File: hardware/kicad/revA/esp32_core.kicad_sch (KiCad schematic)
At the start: 0 parts

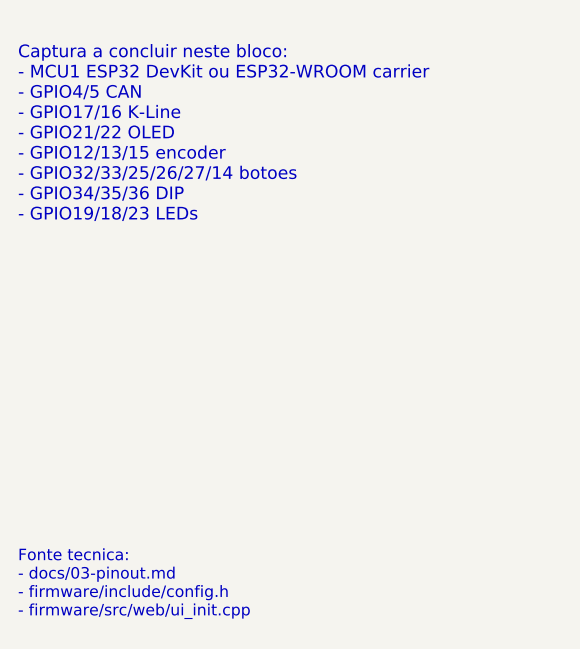
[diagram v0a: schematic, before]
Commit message: feat: persist simulator state and carrier handoff
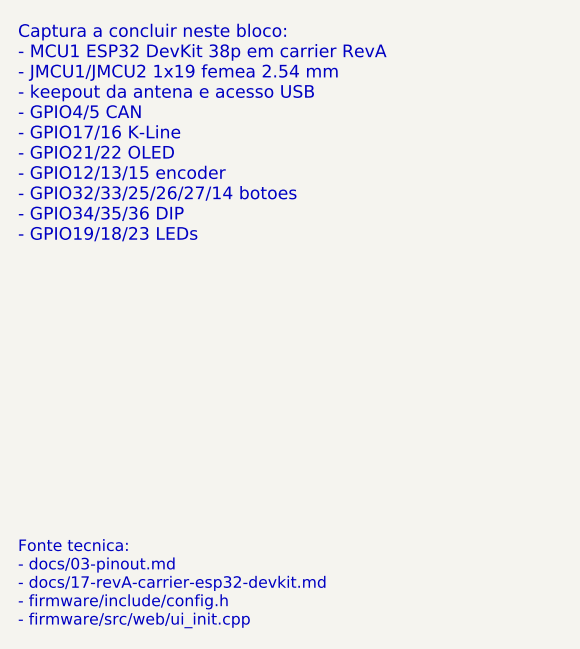
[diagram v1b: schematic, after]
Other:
- note added: "Captura a concluir neste bloco: - MCU1 ESP32 DevKit 38p em carrier RevA - JMCU1/JMCU2 1x19 femea 2.54 mm - keepout da antena e acesso USB - GPIO4/5 CAN - GPIO17/16 K-Line - GPIO21/22 OLED - GPIO12/13/15 encoder - GPIO32/33/25/26/27/14 botoes - GPIO34/35/36 DIP - GPIO19/18/23 LEDs"
- note added: "Fonte tecnica: - docs/03-pinout.md - docs/17-revA-carrier-esp32-devkit.md - firmware/include/config.h - firmware/src/web/ui_init.cpp"
- note removed: "Captura a concluir neste bloco: - MCU1 ESP32 DevKit ou ESP32-WROOM carrier - GPIO4/5 CAN - GPIO17/16 K-Line - GPIO21/22 OLED - GPIO12/13/15 encoder - GPIO32/33/25/26/27/14 botoes - GPIO34/35/36 DIP - GPIO19/18/23 LEDs"
- note removed: "Fonte tecnica: - docs/03-pinout.md - firmware/include/config.h - firmware/src/web/ui_init.cpp"
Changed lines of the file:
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@@
 		(comment 1 "Keep validated GPIO map from firmware/docs")
 	)
-	(text "Captura a concluir neste bloco:\n- MCU1 ESP32 DevKit ou ESP32-WROOM carrier\n- GPIO4/5 CAN\n- GPIO17/16 K-Line\n- GPIO21/22 OLED\n- GPIO12/13/15 encoder\n- GPIO32/33/25/26/27/14 botoes\n- GPIO34/35/36 DIP\n- GPIO19/18/23 LEDs"
+	(text "Captura a concluir neste bloco:\n- MCU1 ESP32 DevKit 38p em carrier RevA\n- JMCU1/JMCU2 1x19 femea 2.54 mm\n- keepout da antena e acesso USB\n- GPIO4/5 CAN\n- GPIO17/16 K-Line\n- GPIO21/22 OLED\n- GPIO12/13/15 encoder\n- GPIO32/33/25/26/27/14 botoes\n- GPIO34/35/36 DIP\n- GPIO19/18/23 LEDs"
 		(exclude_from_sim no)
 		(at 18 20 0)
@@
 		)
 	)
-	(text "Fonte tecnica:\n- docs/03-pinout.md\n- firmware/include/config.h\n- firmware/src/web/ui_init.cpp"
+	(text "Fonte tecnica:\n- docs/03-pinout.md\n- docs/17-revA-carrier-esp32-devkit.md\n- firmware/include/config.h\n- firmware/src/web/ui_init.cpp"
 		(exclude_from_sim no)
 		(at 18 70 0)

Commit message: Align RevA pinout and retire legacy handoff
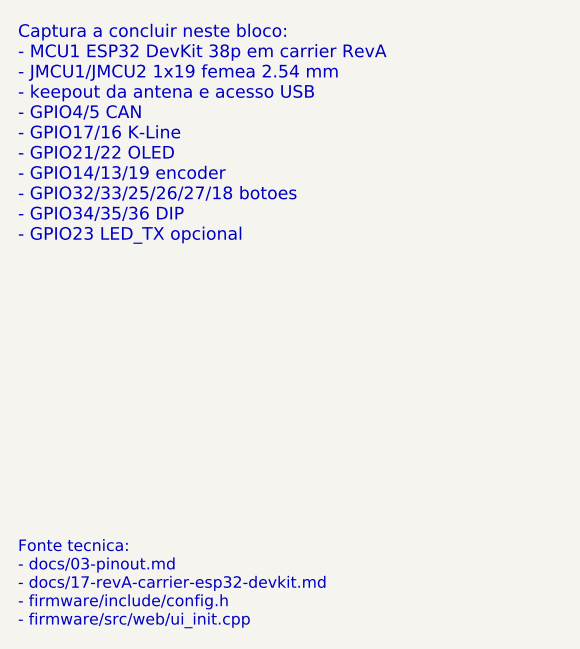
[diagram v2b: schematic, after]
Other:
- note added: "Captura a concluir neste bloco: - MCU1 ESP32 DevKit 38p em carrier RevA - JMCU1/JMCU2 1x19 femea 2.54 mm - keepout da antena e acesso USB - GPIO4/5 CAN - GPIO17/16 K-Line - GPIO21/22 OLED - GPIO14/13/19 encoder - GPIO32/33/25/26/27/18 botoes - GPIO34/35/36 DIP - GPIO23 LED_TX opcional"
- note removed: "Captura a concluir neste bloco: - MCU1 ESP32 DevKit 38p em carrier RevA - JMCU1/JMCU2 1x19 femea 2.54 mm - keepout da antena e acesso USB - GPIO4/5 CAN - GPIO17/16 K-Line - GPIO21/22 OLED - GPIO12/13/15 encoder - GPIO32/33/25/26/27/14 botoes - GPIO34/35/36 DIP - GPIO19/18/23 LEDs"
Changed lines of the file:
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@@
 		(comment 1 "Keep validated GPIO map from firmware/docs")
 	)
-	(text "Captura a concluir neste bloco:\n- MCU1 ESP32 DevKit 38p em carrier RevA\n- JMCU1/JMCU2 1x19 femea 2.54 mm\n- keepout da antena e acesso USB\n- GPIO4/5 CAN\n- GPIO17/16 K-Line\n- GPIO21/22 OLED\n- GPIO12/13/15 encoder\n- GPIO32/33/25/26/27/14 botoes\n- GPIO34/35/36 DIP\n- GPIO19/18/23 LEDs"
+	(text "Captura a concluir neste bloco:\n- MCU1 ESP32 DevKit 38p em carrier RevA\n- JMCU1/JMCU2 1x19 femea 2.54 mm\n- keepout da antena e acesso USB\n- GPIO4/5 CAN\n- GPIO17/16 K-Line\n- GPIO21/22 OLED\n- GPIO14/13/19 encoder\n- GPIO32/33/25/26/27/18 botoes\n- GPIO34/35/36 DIP\n- GPIO23 LED_TX opcional"
 		(exclude_from_sim no)
 		(at 18 20 0)

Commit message: Consolidate docs set and finalize Wi-Fi config updates
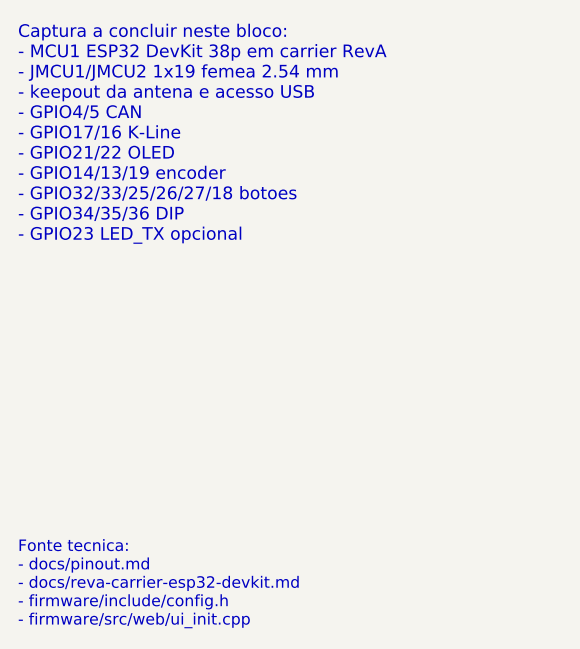
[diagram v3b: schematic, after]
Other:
- note added: "Fonte tecnica: - docs/pinout.md - docs/reva-carrier-esp32-devkit.md - firmware/include/config.h - firmware/src/web/ui_init.cpp"
- note removed: "Fonte tecnica: - docs/03-pinout.md - docs/17-revA-carrier-esp32-devkit.md - firmware/include/config.h - firmware/src/web/ui_init.cpp"
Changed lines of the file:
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@@
 		)
 	)
-	(text "Fonte tecnica:\n- docs/03-pinout.md\n- docs/17-revA-carrier-esp32-devkit.md\n- firmware/include/config.h\n- firmware/src/web/ui_init.cpp"
+(text "Fonte tecnica:\n- docs/pinout.md\n- docs/reva-carrier-esp32-devkit.md\n- firmware/include/config.h\n- firmware/src/web/ui_init.cpp"
 		(exclude_from_sim no)
 		(at 18 70 0)
